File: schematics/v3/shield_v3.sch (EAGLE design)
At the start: 34 parts, among them Q2 PMV20EN, Q3 PMV20EN, Q4 PMV20EN, Q5 PMV20EN, U1 ATMEGA168

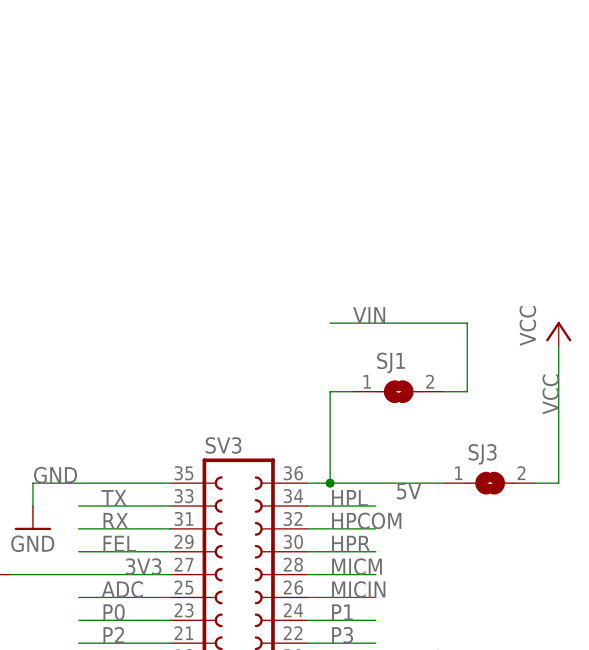
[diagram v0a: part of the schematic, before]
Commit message: Added jumper to drive atmega via Vin or CHIP 5V or CHIP3.3V
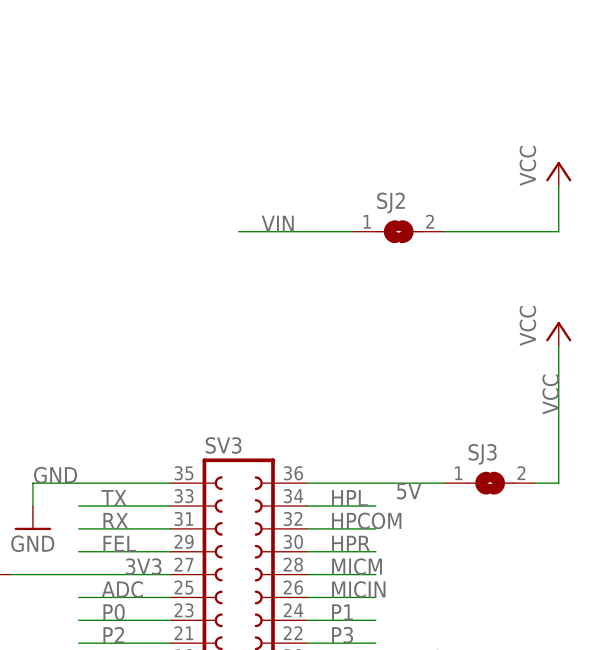
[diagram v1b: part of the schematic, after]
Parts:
- removed SJ1: (no value), jumper:SJ
- added SJ2: (no value), jumper:SJ
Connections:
- net 5V: no longer SJ1.1
- net VCC: now also SJ2.2
- net VIN: now also SJ2.1; no longer SJ1.2
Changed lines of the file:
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@@
 <?xml version="1.0" encoding="utf-8"?>
 <!DOCTYPE eagle SYSTEM "eagle.dtd">
-<eagle version="6.5.0">
+<eagle version="7.5.0">
 <drawing>
 <settings>
@@
 <part name="P+8" library="supply1" deviceset="VCC" device=""/>
 <part name="GND9" library="supply1" deviceset="GND" device=""/>
-<part name="SJ1" library="jumper" deviceset="SJ" device=""/>
 <part name="GND1" library="supply1" deviceset="GND" device=""/>
 <part name="PAD8" library="wirepad" deviceset="SMD5" device=""/>
@@
 <part name="PAD13" library="wirepad" deviceset="SMD2" device=""/>
 <part name="R2" library="rcl" deviceset="R-EU_" device="M1206"/>
+<part name="SJ2" library="jumper" deviceset="SJ" device=""/>
+<part name="P+2" library="supply1" deviceset="VCC" device=""/>
 </parts>
 <sheets>
@@
 <instance part="P+8" gate="VCC" x="370.84" y="101.6"/>
 <instance part="GND9" gate="1" x="312.42" y="78.74"/>
-<instance part="SJ1" gate="1" x="353.06" y="93.98"/>
 <instance part="GND1" gate="1" x="363.22" y="53.34"/>
 <instance part="PAD8" gate="1" x="99.06" y="73.66"/>
@@
 <instance part="PAD13" gate="1" x="71.12" y="60.96"/>
 <instance part="R2" gate="G$1" x="71.12" y="-2.54" rot="R180"/>
+<instance part="SJ2" gate="1" x="353.06" y="111.76"/>
+<instance part="P+2" gate="VCC" x="370.84" y="119.38"/>
 </instances>
 <busses>
@@
 <pinref part="P+8" gate="VCC" pin="VCC"/>
 </segment>
+<segment>
+<pinref part="SJ2" gate="1" pin="2"/>
+<wire x1="358.14" y1="111.76" x2="370.84" y2="111.76" width="0.1524" layer="91"/>
+<wire x1="370.84" y1="111.76" x2="370.84" y2="116.84" width="0.1524" layer="91"/>
+<pinref part="P+2" gate="VCC" pin="VCC"/>
+</segment>
 </net>
 <net name="OC0_PWM1" class="0">
@@
 </segment>
 <segment>
-<pinref part="SJ1" gate="1" pin="2"/>
-<wire x1="358.14" y1="93.98" x2="360.68" y2="93.98" width="0.1524" layer="91"/>
-<wire x1="360.68" y1="93.98" x2="360.68" y2="101.6" width="0.1524" layer="91"/>
-<wire x1="360.68" y1="101.6" x2="345.44" y2="101.6" width="0.1524" layer="91"/>
-<label x="347.98" y="101.6" size="1.778" layer="95"/>
+<pinref part="SJ2" gate="1" pin="1"/>
+<wire x1="347.98" y1="111.76" x2="335.28" y2="111.76" width="0.1524" layer="91"/>
+<label x="337.82" y="111.76" size="1.778" layer="95"/>
 </segment>
 </net>
@@
 <pinref part="SJ3" gate="1" pin="1"/>
 <pinref part="SV3" gate="G$1" pin="36"/>
-<wire x1="342.9" y1="83.82" x2="345.44" y2="83.82" width="0.1524" layer="91"/>
-<wire x1="345.44" y1="83.82" x2="358.14" y2="83.82" width="0.1524" layer="91"/>
-<wire x1="345.44" y1="83.82" x2="345.44" y2="93.98" width="0.1524" layer="91"/>
-<pinref part="SJ1" gate="1" pin="1"/>
-<wire x1="345.44" y1="93.98" x2="347.98" y2="93.98" width="0.1524" layer="91"/>
-<junction x="345.44" y="83.82"/>
-</segment>
-</net>
+<wire x1="342.9" y1="83.82" x2="358.14" y2="83.82" width="0.1524" layer="91"/>
+</segment>
+</net>
